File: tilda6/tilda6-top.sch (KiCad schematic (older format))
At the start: 19 parts, among them J1 Conn_02x14_Odd_Even, J2 Conn_02x02_Odd_Even, J3 Conn_02x02_Odd_Even, J4 Conn_01x13, J5 Conn_01x08, J6 Conn_01x08, Q1 LP0404N3T5G, Q2 LP0404N3T5G, SW1 SW_Push, SW2 SW_Push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

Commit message: Implement most of martling's recommendations: - power switch now controls DC/DC enable - top board caps changed from 1x4.7u to 1x1u+1x10n - top board edge via stitching - bottom board ground all around edge where possible - changed UVLO monitor threshold to 3.3V - all outermost traces very close to edge are now gnd not implemented: VBUS ferrite
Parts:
- added C3, C4: 10n, Capacitor_SMD:C_0402_1005Metric, symbol Device:C
- C1, C2: value 4.7u -> 1u
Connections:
- net 3V3: now also C3.1
- net DISPLAY_3V3: now also C4.1
- net GND: now also C3.2, C4.2
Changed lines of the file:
@@
 P 4450 4400
 F 0 "C1" H 4565 4446 50  0000 L CNN
-F 1 "4.7u" H 4565 4355 50  0000 L CNN
+F 1 "1u" H 4565 4355 50  0000 L CNN
 F 2 "Capacitor_SMD:C_0402_1005Metric" H 4488 4250 50  0001 C CNN
 F 3 "~" H 4450 4400 50  0001 C CNN
@@
 P 4850 4400
 F 0 "C2" H 4965 4446 50  0000 L CNN
-F 1 "4.7u" H 4965 4355 50  0000 L CNN
+F 1 "1u" H 4965 4355 50  0000 L CNN
 F 2 "Capacitor_SMD:C_0402_1005Metric" H 4888 4250 50  0001 C CNN
 F 3 "~" H 4850 4400 50  0001 C CNN
@@
 Text Label 4850 4250 2    50   ~ 0
 3V3
+$Comp
+L Device:C C3
+U 1 1 620D9A27
+P 5200 4400
+F 0 "C3" H 5315 4446 50  0000 L CNN
+F 1 "10n" H 5315 4355 50  0000 L CNN
+F 2 "Capacitor_SMD:C_0402_1005Metric" H 5238 4250 50  0001 C CNN
+F 3 "~" H 5200 4400 50  0001 C CNN
+	1    5200 4400
+	1    0    0    -1
+$EndComp
+$Comp
+L Device:C C4
+U 1 1 620DA462
+P 5600 4400
+F 0 "C4" H 5715 4446 50  0000 L CNN
+F 1 "10n" H 5715 4355 50  0000 L CNN
+F 2 "Capacitor_SMD:C_0402_1005Metric" H 5638 4250 50  0001 C CNN
+F 3 "~" H 5600 4400 50  0001 C CNN
+	1    5600 4400
+	1    0    0    -1
+$EndComp
+Wire Wire Line
+	4850 4550 5200 4550
+Connection ~ 5200 4550
+Wire Wire Line
+	5200 4550 5600 4550
+Text Label 5200 4250 2    50   ~ 0
+3V3
+Text Label 5600 4250 0    50   ~ 0
+DISPLAY_3V3
 $EndSCHEMATC

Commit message: Add new tilda6-bot board with IC instead of module, and martling-compatible layout
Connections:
- net 3V3: now also J3.4 (Pin_4); no longer J3.3 (Pin_3)
- net BATTERY+: now also J3.2 (Pin_2); no longer J3.4 (Pin_4)
- net GND: now also J3.1 (Pin_1); no longer J3.2 (Pin_2)
- no-connect marks 4 -> 9
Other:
- moved on the sheet: J3
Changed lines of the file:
@@
-$EndComp
-$Comp
-L Connector_Generic:Conn_02x02_Odd_Even J3
-U 1 1 61F5E010
-P 2600 3400
-F 0 "J3" H 2650 3617 50  0000 C CNN
-F 1 "Conn_02x02_Odd_Even" H 2650 3526 50  0000 C CNN
-F 2 "Connector_PinHeader_1.27mm:PinHeader_2x02_P1.27mm_Vertical_SMD" H 2600 3400 50  0001 C CNN
-F 3 "~" H 2600 3400 50  0001 C CNN
-	1    2600 3400
-	1    0    0    -1
 $EndComp
 $Comp
@@
 Text Label 2650 4350 0    50   ~ 0
 GND
-Text Label 2400 3500 2    50   ~ 0
-3V3
-Text Label 2900 3400 0    50   ~ 0
+Text Label 2600 3700 2    50   ~ 0
+3V3
+Text Label 2700 3200 0    50   ~ 0
 GND
 Wire Wire Line
 	2650 4050 2900 4050
 Wire Wire Line
-	2900 4050 2900 3500
+	2900 4050 2900 3700
 $Comp
 L Switch:SW_Push SW2
@@
 Text Label 5600 4250 0    50   ~ 0
 DISPLAY_3V3
+$Comp
+L Connector_Generic:Conn_02x02_Odd_Even J3
+U 1 1 61F5E010
+P 2700 3400
+F 0 "J3" H 2750 3617 50  0000 C CNN
+F 1 "Conn_02x02_Odd_Even" H 2750 3526 50  0000 C CNN
+F 2 "Connector_PinHeader_1.27mm:PinHeader_2x02_P1.27mm_Vertical_SMD" H 2700 3400 50  0001 C CNN
+F 3 "~" H 2700 3400 50  0001 C CNN
+	1    2700 3400
+	0    1    1    0
+$EndComp
+Wire Wire Line
+	2700 3700 2900 3700
+NoConn ~ 2600 3200
+NoConn ~ 2400 2850
+NoConn ~ 2400 2950
+NoConn ~ 2900 2850
+NoConn ~ 2900 2950
 $EndSCHEMATC

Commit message: Use correct footprint for top PCB FPC connector and add 3d model for it
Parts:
- J5, J6: footprint Connector_FFC-FPC:Hirose_FH12-8S-0.5SH_1x08-1MP_P0.50mm_Horizontal -> tilda6:XUNPU_FPC-05F-8PH20
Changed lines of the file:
@@
 F 0 "J5" H 3780 4442 50  0000 L CNN
 F 1 "Conn_01x08" H 3780 4351 50  0000 L CNN
-F 2 "Connector_FFC-FPC:Hirose_FH12-8S-0.5SH_1x08-1MP_P0.50mm_Horizontal" H 3700 4450 50  0001 C CNN
+F 2 "tilda6:XUNPU_FPC-05F-8PH20" H 3700 4450 50  0001 C CNN
 F 3 "~" H 3700 4450 50  0001 C CNN
 	1    3700 4450
@@
 F 0 "J6" H 3780 5392 50  0000 L CNN
 F 1 "Conn_01x08" H 3780 5301 50  0000 L CNN
-F 2 "Connector_FFC-FPC:Hirose_FH12-8S-0.5SH_1x08-1MP_P0.50mm_Horizontal" H 3700 5400 50  0001 C CNN
+F 2 "tilda6:XUNPU_FPC-05F-8PH20" H 3700 5400 50  0001 C CNN
 F 3 "~" H 3700 5400 50  0001 C CNN
 	1    3700 5400

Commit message: Swap out undervoltage monitor, replace topside switches with cheaper part
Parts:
- SW2, SW3: footprint Button_Switch_SMD:SW_SPST_B3U-1000P -> tilda6:TS3735PA_250gf
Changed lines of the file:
@@
 F 0 "SW2" H 1750 2535 50  0000 C CNN
 F 1 "SW_Push" H 1750 2444 50  0000 C CNN
-F 2 "Button_Switch_SMD:SW_SPST_B3U-1000P" H 1750 2450 50  0001 C CNN
+F 2 "tilda6:TS3735PA_250gf" H 1750 2450 50  0001 C CNN
 F 3 "~" H 1750 2450 50  0001 C CNN
 	1    1750 2250
@@
 F 0 "SW3" H 1750 2935 50  0000 C CNN
 F 1 "SW_Push" H 1750 2844 50  0000 C CNN
-F 2 "Button_Switch_SMD:SW_SPST_B3U-1000P" H 1750 2850 50  0001 C CNN
+F 2 "tilda6:TS3735PA_250gf" H 1750 2850 50  0001 C CNN
 F 3 "~" H 1750 2850 50  0001 C CNN
 	1    1750 2650

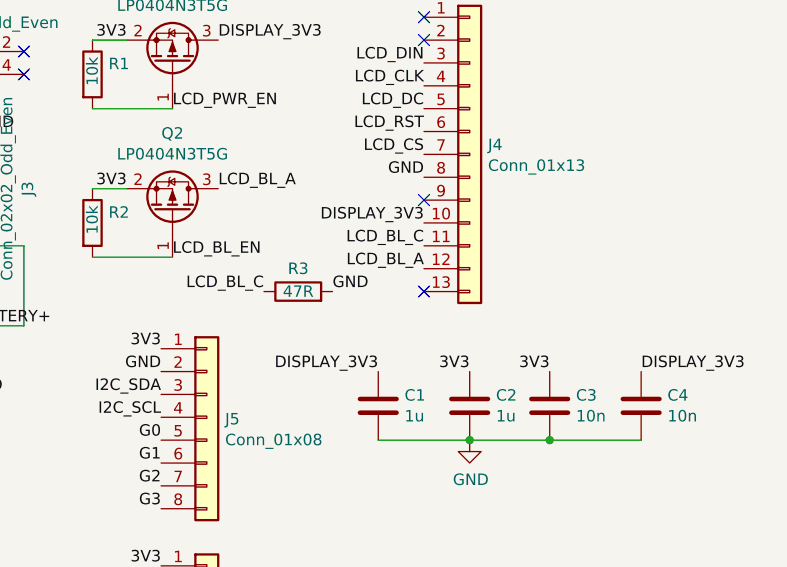
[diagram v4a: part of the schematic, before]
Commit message: correct assumptions about display flex curvature
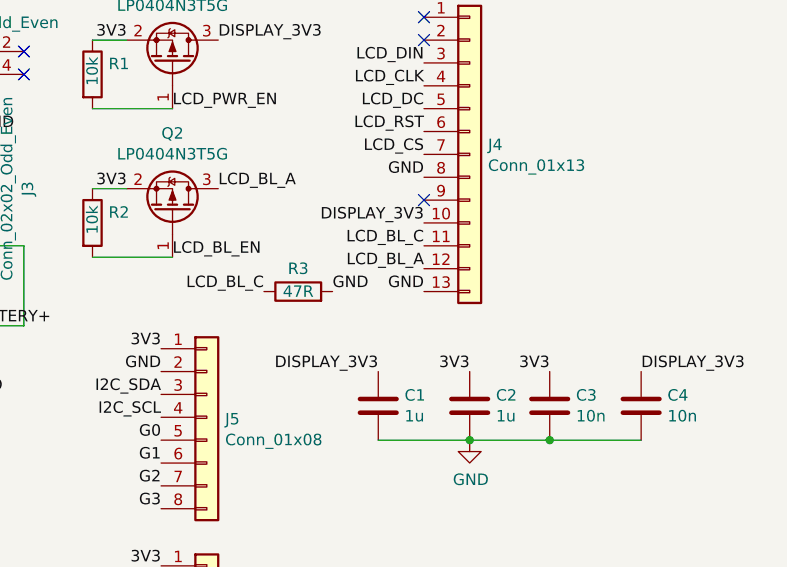
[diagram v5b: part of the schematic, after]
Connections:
- net GND: now also J4.13 (Pin_13)
- no-connect marks 9 -> 8
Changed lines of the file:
@@
 NoConn ~ 4650 2800
 NoConn ~ 4650 3500
-NoConn ~ 4650 3900
 Text Label 4650 2900 2    50   ~ 0
 LCD_DIN
@@
 NoConn ~ 2900 2850
 NoConn ~ 2900 2950
+Text Label 4650 3900 2    50   ~ 0
+GND
 $EndSCHEMATC

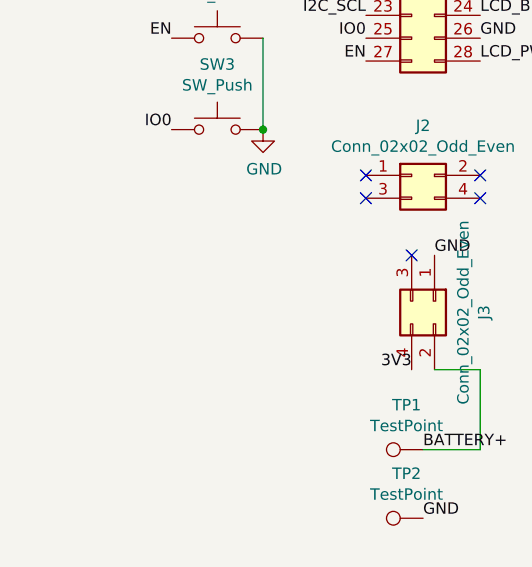
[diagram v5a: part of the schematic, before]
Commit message: Add battery connector to top PCB
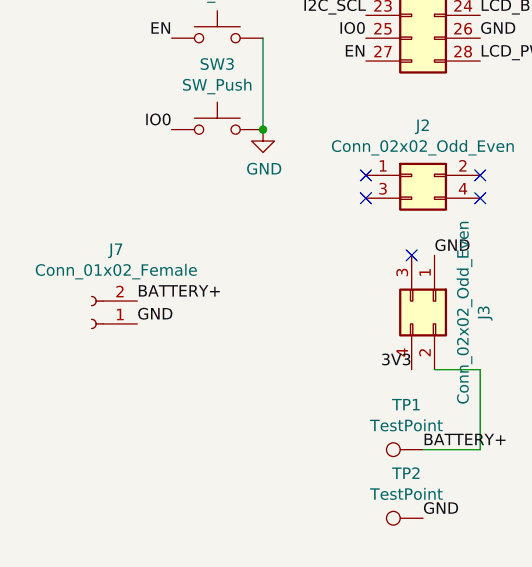
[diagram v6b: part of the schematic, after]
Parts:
- added J7: Conn_01x02_Female, Connector_JST:JST_SH_SM02B-SRSS-TB_1x02-1MP_P1.00mm_Horizontal, symbol Connector:Conn_01x02_Female
- J4: footprint corelib:ER-TFT-1.14-reverse -> corelib:ER-TFT-1.14
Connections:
- net BATTERY+: now also J7.2 (Pin_2)
- net GND: now also J7.1 (Pin_1)
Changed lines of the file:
@@
 F 0 "J4" H 4930 3342 50  0000 L CNN
 F 1 "Conn_01x13" H 4930 3251 50  0000 L CNN
-F 2 "corelib:ER-TFT-1.14-reverse" H 4850 3300 50  0001 C CNN
+F 2 "corelib:ER-TFT-1.14" H 4850 3300 50  0001 C CNN
 F 3 "~" H 4850 3300 50  0001 C CNN
 	1    4850 3300
@@
 Text Label 4650 3900 2    50   ~ 0
 GND
+$Comp
+L Connector:Conn_01x02_Female J7
+U 1 1 624964CC
+P 1200 3500
+F 0 "J7" H 1092 3175 50  0000 C CNN
+F 1 "Conn_01x02_Female" H 1092 3266 50  0000 C CNN
+F 2 "Connector_JST:JST_SH_SM02B-SRSS-TB_1x02-1MP_P1.00mm_Horizontal" H 1200 3500 50  0001 C CNN
+F 3 "~" H 1200 3500 50  0001 C CNN
+	1    1200 3500
+	-1   0    0    1
+$EndComp
+Text Label 1400 3400 0    50   ~ 0
+BATTERY+
+Text Label 1400 3500 0    50   ~ 0
+GND
 $EndSCHEMATC

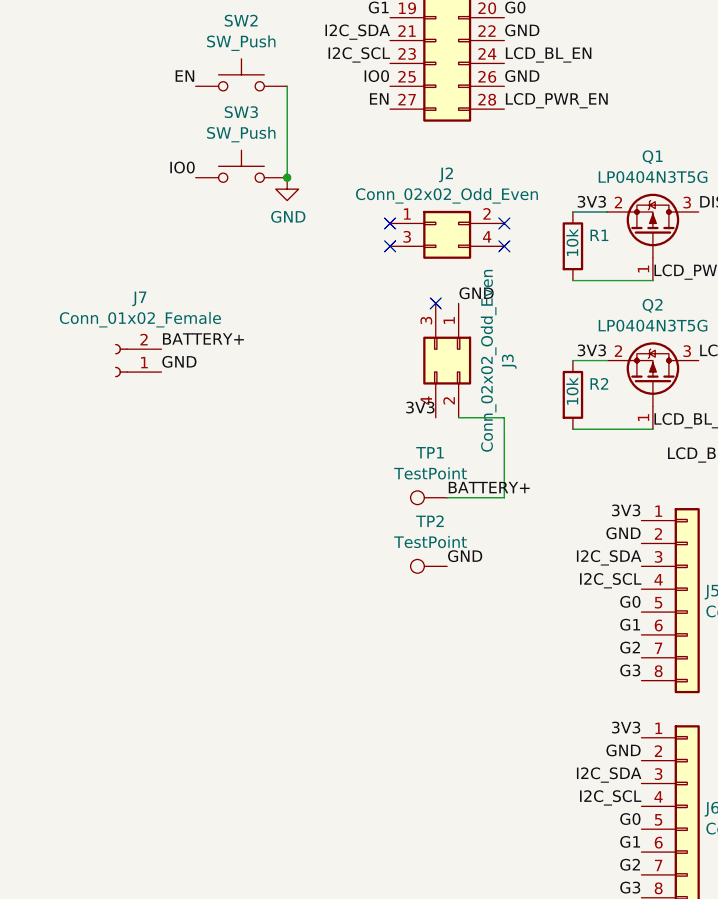
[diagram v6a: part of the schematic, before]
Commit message: Flip battery connector pinout to match off the shelf batteries. Add USB connector breakout to top PCB.
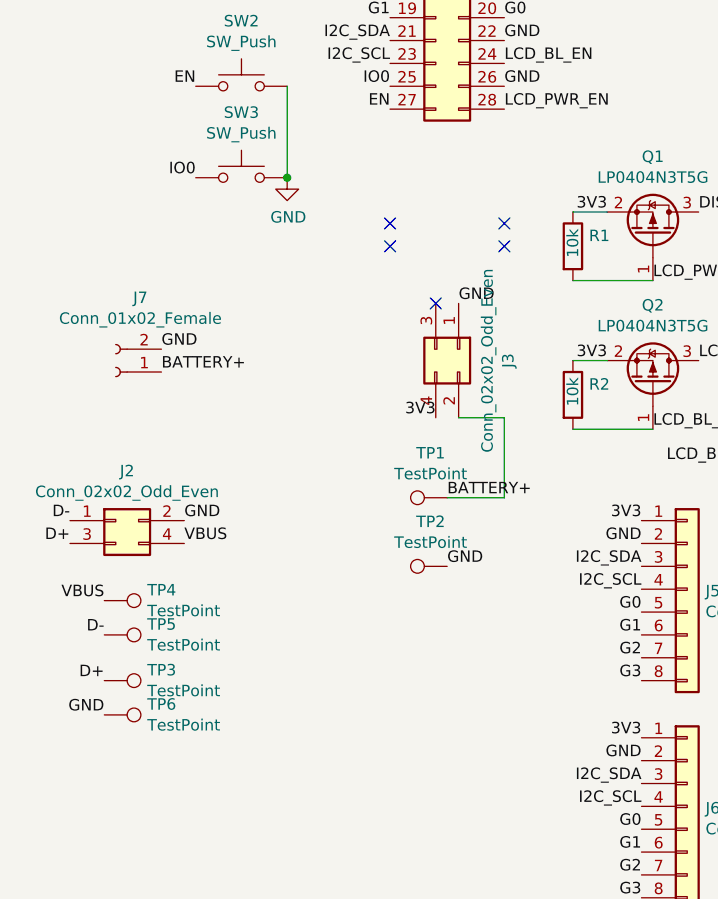
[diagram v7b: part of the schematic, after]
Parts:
- added TP3, TP4, TP5, TP6: TestPoint, TestPoint:TestPoint_Pad_1.5x1.5mm, symbol Connector:TestPoint
- SW2, SW3: footprint tilda6:TS3735PA_250gf -> Button_Switch_SMD:SW_Push_1P1T_NO_CK_KMR2
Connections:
- net BATTERY+: now also J7.1 (Pin_1); no longer J7.2 (Pin_2)
- net GND: now also J2.2 (Pin_2), J7.2 (Pin_2), TP6.1; no longer J7.1 (Pin_1)
- net D-: now reaches J2.1 (Pin_1)
- net D-: now also TP5.1
- net D+: now reaches J2.3 (Pin_3)
- net D+: now also TP3.1
- net VBUS: now reaches J2.4 (Pin_4)
- net VBUS: now also TP4.1
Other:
- moved on the sheet: J2
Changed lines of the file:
@@
 L Connector_Generic:Conn_02x02_Odd_Even J2
 U 1 1 61F5DC37
-P 2600 2850
-F 0 "J2" H 2650 3067 50  0000 C CNN
-F 1 "Conn_02x02_Odd_Even" H 2650 2976 50  0000 C CNN
-F 2 "Connector_PinHeader_1.27mm:PinHeader_2x02_P1.27mm_Vertical_SMD" H 2600 2850 50  0001 C CNN
-F 3 "~" H 2600 2850 50  0001 C CNN
-	1    2600 2850
+P 1200 4150
+F 0 "J2" H 1250 4367 50  0000 C CNN
+F 1 "Conn_02x02_Odd_Even" H 1250 4276 50  0000 C CNN
+F 2 "Connector_PinHeader_1.27mm:PinHeader_2x02_P1.27mm_Vertical_SMD" H 1200 4150 50  0001 C CNN
+F 3 "~" H 1200 4150 50  0001 C CNN
+	1    1200 4150
 	1    0    0    -1
 $EndComp
@@
 F 0 "SW2" H 1750 2535 50  0000 C CNN
 F 1 "SW_Push" H 1750 2444 50  0000 C CNN
-F 2 "tilda6:TS3735PA_250gf" H 1750 2450 50  0001 C CNN
+F 2 "Button_Switch_SMD:SW_Push_1P1T_NO_CK_KMR2" H 1750 2450 50  0001 C CNN
 F 3 "~" H 1750 2450 50  0001 C CNN
 	1    1750 2250
@@
 F 0 "SW3" H 1750 2935 50  0000 C CNN
 F 1 "SW_Push" H 1750 2844 50  0000 C CNN
-F 2 "tilda6:TS3735PA_250gf" H 1750 2850 50  0001 C CNN
+F 2 "Button_Switch_SMD:SW_Push_1P1T_NO_CK_KMR2" H 1750 2850 50  0001 C CNN
 F 3 "~" H 1750 2850 50  0001 C CNN
 	1    1750 2650
@@
 	-1   0    0    1
 $EndComp
+Text Label 1400 3500 0    50   ~ 0
+BATTERY+
 Text Label 1400 3400 0    50   ~ 0
-BATTERY+
-Text Label 1400 3500 0    50   ~ 0
+GND
+Text Label 1000 4150 2    50   ~ 0
+D-
+Text Label 1000 4250 2    50   ~ 0
+D+
+Text Label 1500 4150 0    50   ~ 0
+GND
+Text Label 1500 4250 0    50   ~ 0
+VBUS
+$Comp
+L Connector:TestPoint TP3
+U 1 1 62514A48
+P 1150 4850
+F 0 "TP3" V 1104 5038 50  0000 L CNN
+F 1 "TestPoint" V 1195 5038 50  0000 L CNN
+F 2 "TestPoint:TestPoint_Pad_1.5x1.5mm" H 1350 4850 50  0001 C CNN
+F 3 "~" H 1350 4850 50  0001 C CNN
+	1    1150 4850
+	0    1    1    0
+$EndComp
+$Comp
+L Connector:TestPoint TP4
+U 1 1 62515446
+P 1150 4500
+F 0 "TP4" V 1104 4688 50  0000 L CNN
+F 1 "TestPoint" V 1195 4688 50  0000 L CNN
+F 2 "TestPoint:TestPoint_Pad_1.5x1.5mm" H 1350 4500 50  0001 C CNN
+F 3 "~" H 1350 4500 50  0001 C CNN
+	1    1150 4500
+	0    1    1    0
+$EndComp
+$Comp
+L Connector:TestPoint TP5
+U 1 1 62515682
+P 1150 4650
+F 0 "TP5" V 1104 4838 50  0000 L CNN
+F 1 "TestPoint" V 1195 4838 50  0000 L CNN
+F 2 "TestPoint:TestPoint_Pad_1.5x1.5mm" H 1350 4650 50  0001 C CNN
+F 3 "~" H 1350 4650 50  0001 C CNN
+	1    1150 4650
+	0    1    1    0
+$EndComp
+$Comp
+L Connector:TestPoint TP6
+U 1 1 625159BC
+P 1150 5000
+F 0 "TP6" V 1104 5188 50  0000 L CNN
+F 1 "TestPoint" V 1195 5188 50  0000 L CNN
+F 2 "TestPoint:TestPoint_Pad_1.5x1.5mm" H 1350 5000 50  0001 C CNN
+F 3 "~" H 1350 5000 50  0001 C CNN
+	1    1150 5000
+	0    1    1    0
+$EndComp
+Text Label 1150 4500 2    50   ~ 0
+VBUS
+Text Label 1150 4650 2    50   ~ 0
+D-
+Text Label 1150 4850 2    50   ~ 0
+D+
+Text Label 1150 5000 2    50   ~ 0
 GND
 $EndSCHEMATC
